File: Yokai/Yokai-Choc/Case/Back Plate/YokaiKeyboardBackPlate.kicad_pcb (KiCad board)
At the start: 2 copper layers, 161.8 x 114.7 mm, 6 parts

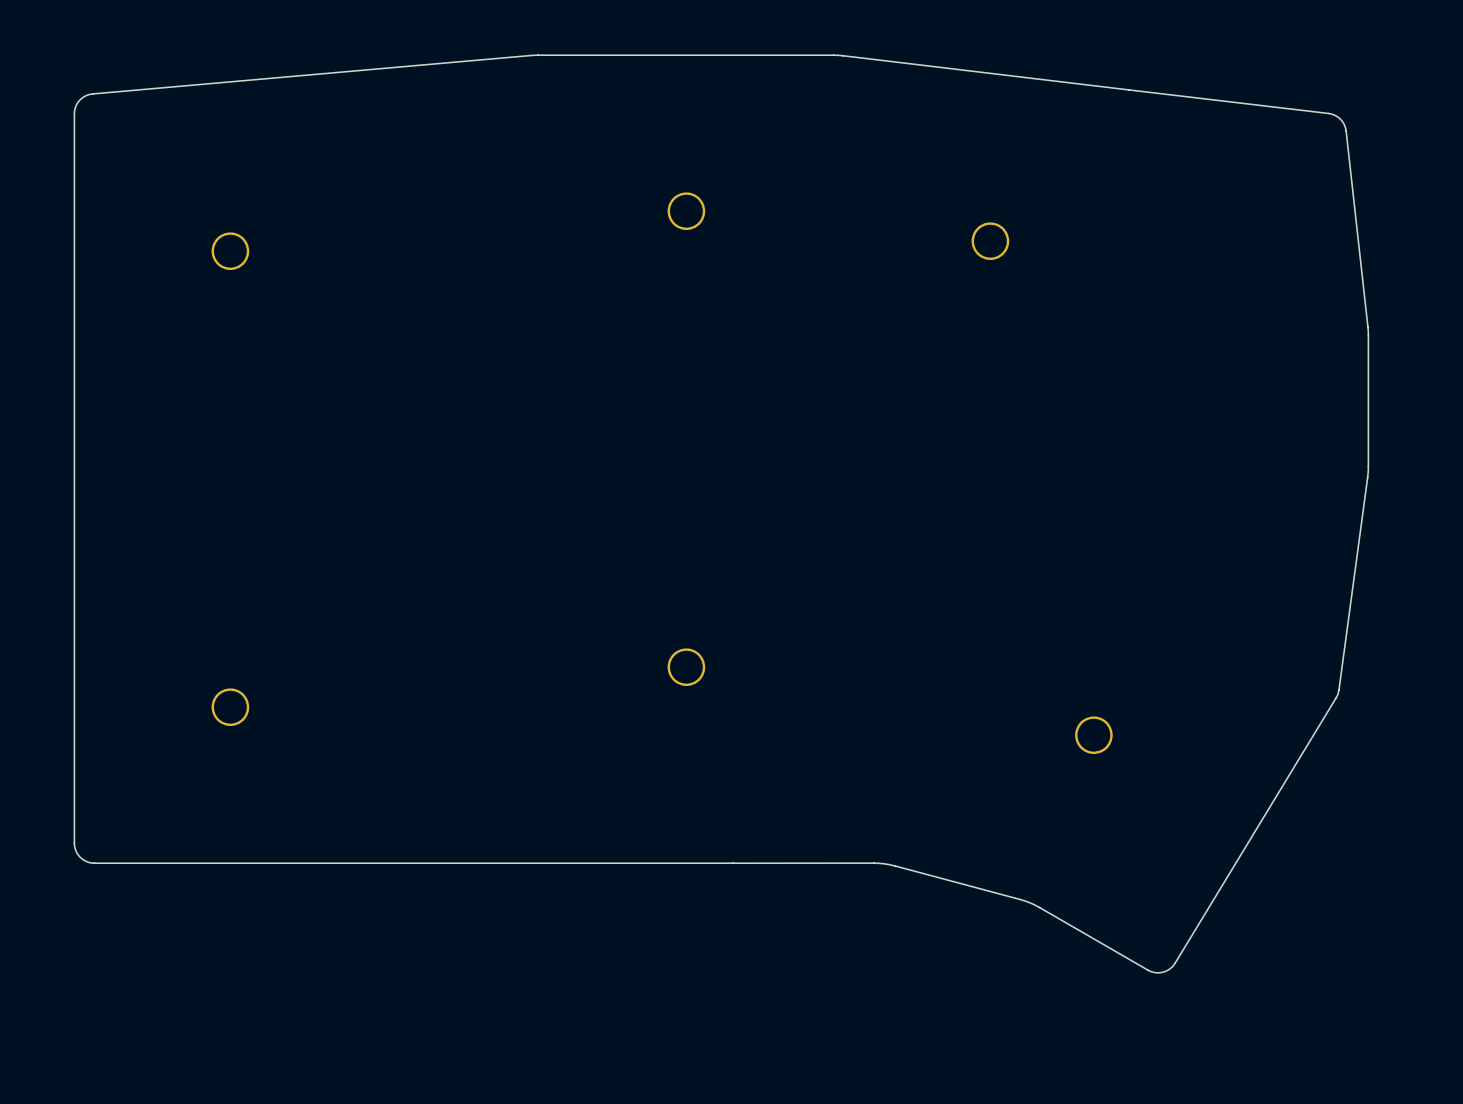
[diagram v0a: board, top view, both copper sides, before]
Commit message: Add files via upload
*Increased pinky stagger
*Inverted stabilizer cutouts
*Added additional thumb key
*Minor footprint changes
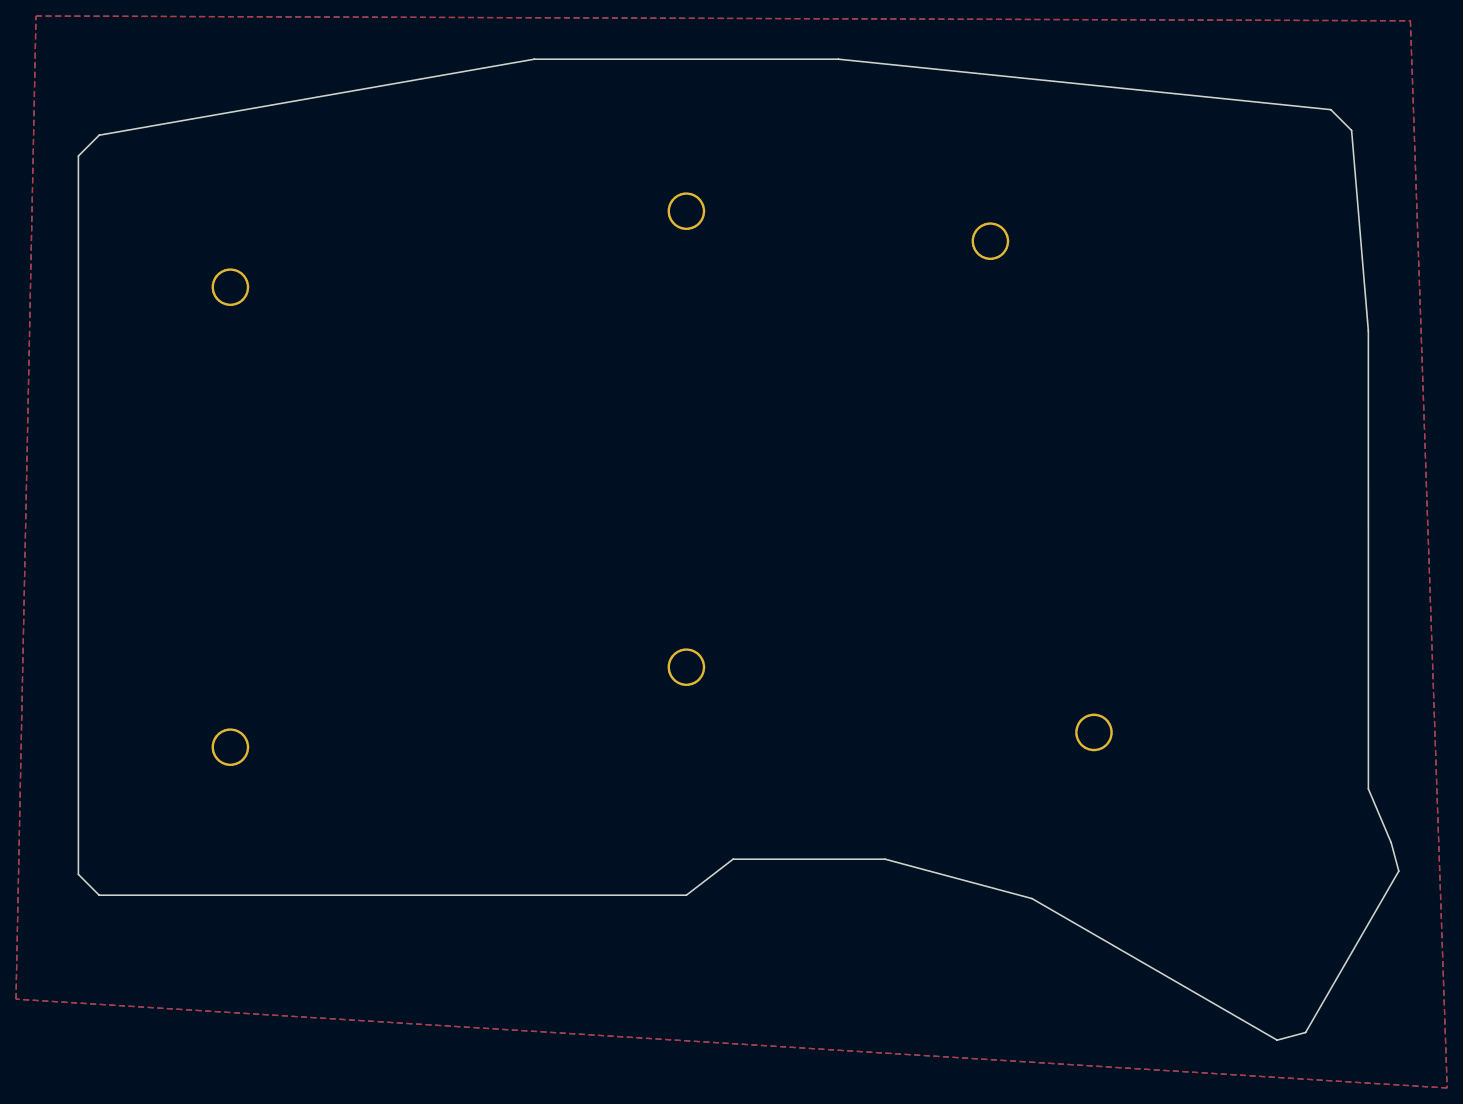
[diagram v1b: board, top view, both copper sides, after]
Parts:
- removed the TH5 at (186.9, 119.5)
- removed the TH5 at (79.0, 116.0)
- removed the TH5 at (79.0, 59.0)
- added TH5: HOLE, kbd:HOLE_M2_TH, F.Cu at (186.9, 119.2)
- added TH5: HOLE, kbd:HOLE_M2_TH, F.Cu at (79.0, 121.0)
- added TH5: HOLE, kbd:HOLE_M2_TH, F.Cu at (79.0, 63.5)
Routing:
- added copper zone on B.Cu, net (none)
- added copper zone on F.Cu, net (none)
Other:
- board size 161.8 x 114.7 mm -> 165.1 x 122.6 mm
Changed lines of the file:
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@@
   (general
     (thickness 1.6)
-    (drawings 30)
+    (drawings 18)
     (tracks 0)
     (zones 0)
@@
   )
   (module kbd:HOLE_M2_TH (layer F.Cu)
-    (at 186.936576 119.50096)
+    (at 186.947906 119.154041)
     (fp_text reference TH5 (at 0 -2.54) (layer F.SilkS) hide
       (effects (font (size 0.29972 0.29972) (thickness 0.0762)))
@@
   )
   (module kbd:HOLE_M2_TH (layer F.Cu)
-    (at 79 116)
-    (fp_text reference TH5 (at 0 -2.54) (layer F.SilkS) hide
-      (effects (font (size 0.29972 0.29972) (thickness 0.0762)))
-    )
-    (fp_text value HOLE (at 0 2.54) (layer F.SilkS) hide
-      (effects (font (size 0.29972 0.29972) (thickness 0.0762)))
-    )
-    (pad "" thru_hole circle (at 0 0 90) (size 4.7 4.7) (drill 4.1) (layers *.Cu *.Mask Dwgs.User)
-      (clearance 0.3))
-  )
-  (module kbd:HOLE_M2_TH (layer F.Cu)
-    (at 79 59)
-    (fp_text reference TH5 (at 0 -2.54) (layer F.SilkS) hide
-      (effects (font (size 0.29972 0.29972) (thickness 0.0762)))
-    )
-    (fp_text value HOLE (at 0 2.54) (layer F.SilkS) hide
-      (effects (font (size 0.29972 0.29972) (thickness 0.0762)))
-    )
-    (pad "" thru_hole circle (at 0 0 90) (size 4.7 4.7) (drill 4.1) (layers *.Cu *.Mask Dwgs.User)
-      (clearance 0.3))
-  )
-  (gr_circle (center 136 54) (end 137.282779 54) (layer Eco1.User) (width 0.2))
-  (gr_circle (center 186.936576 119.50096) (end 188.219356 119.50096) (layer Eco1.User) (width 0.2))
-  (gr_circle (center 136 111) (end 137.282779 111) (layer Eco1.User) (width 0.2))
-  (gr_circle (center 174 57.75) (end 175.282779 57.75) (layer Eco1.User) (width 0.2))
-  (gr_circle (center 79 116) (end 80.282779 116) (layer Eco1.User) (width 0.2))
-  (gr_circle (center 79 59) (end 80.282779 59) (layer Eco1.User) (width 0.2))
-  (gr_arc (start 215.982233 44.267766) (end 218.466903 43.991339) (angle -76.92360867) (layer Edge.Cuts) (width 0.2))
-  (gr_line (start 218.466903 43.991339) (end 221.188682 68.456026) (layer Edge.Cuts) (width 0.2))
-  (gr_line (start 216.275129 41.784983) (end 191.296693 38.83825) (layer Edge.Cuts) (width 0.2))
-  (gr_arc (start 211.25 69.561737) (end 221.25 69.561737) (angle -6.348242205) (layer Edge.Cuts) (width 0.2))
-  (gr_line (start 221.25 69.561737) (end 221.25 85.92804) (layer Edge.Cuts) (width 0.2))
-  (gr_arc (start 211.25 85.92804) (end 221.1601 87.265918) (angle -7.688527176) (layer Edge.Cuts) (width 0.2))
-  (gr_line (start 221.1601 87.265918) (end 217.569781 113.860593) (layer Edge.Cuts) (width 0.2))
-  (gr_arc (start 117.437756 44.5) (end 117.437756 34.5) (angle -5.013113755) (layer Edge.Cuts) (width 0.2))
-  (gr_line (start 61.78154 39.343724) (end 116.563918 34.538252) (layer Edge.Cuts) (width 0.2))
-  (gr_line (start 117.437756 34.5) (end 154.404509 34.5) (layer Edge.Cuts) (width 0.2))
-  (gr_arc (start 154.404509 44.5) (end 155.591281 34.570671) (angle -6.815768334) (layer Edge.Cuts) (width 0.2))
-  (gr_line (start 155.591281 34.570671) (end 191.296693 38.83825) (layer Edge.Cuts) (width 0.2))
-  (gr_arc (start 159.45792 145.496019) (end 162.04611 135.836761) (angle -15.01294376) (layer Edge.Cuts) (width 0.2))
-  (gr_line (start 177.727072 140.038462) (end 162.04611 135.836761) (layer Edge.Cuts) (width 0.2))
-  (gr_line (start 159.455661 135.49602) (end 141.838598 135.5) (layer Edge.Cuts) (width 0.2))
-  (gr_arc (start 175.138881 149.69772) (end 180.140837 141.038596) (angle -15.01294376) (layer Edge.Cuts) (width 0.2))
-  (gr_line (start 193.700875 148.871573) (end 180.140837 141.038596) (layer Edge.Cuts) (width 0.2))
-  (gr_arc (start 215.092256 113.526124) (end 217.229354 114.823356) (angle -23.5695086) (layer Edge.Cuts) (width 0.2))
-  (gr_line (start 217.229354 114.823356) (end 197.088462 148.004024) (layer Edge.Cuts) (width 0.2))
-  (gr_arc (start 62 133) (end 59.5 133) (angle -90) (layer Edge.Cuts) (width 0.2))
-  (gr_line (start 59.5 41.834161) (end 59.5 133) (layer Edge.Cuts) (width 0.2))
-  (gr_line (start 141.838598 135.5) (end 62 135.5) (layer Edge.Cuts) (width 0.2))
-  (gr_arc (start 194.951365 146.706792) (end 193.700875 148.871573) (angle -88.75490799) (layer Edge.Cuts) (width 0.2))
-  (gr_arc (start 62 41.834161) (end 61.78154 39.343724) (angle -84.98688624) (layer Edge.Cuts) (width 0.2))
+    (at 79 121)
+    (fp_text reference TH5 (at 0 -2.54) (layer F.SilkS) hide
+      (effects (font (size 0.29972 0.29972) (thickness 0.0762)))
+    )
+    (fp_text value HOLE (at 0 2.54) (layer F.SilkS) hide
+      (effects (font (size 0.29972 0.29972) (thickness 0.0762)))
+    )
+    (pad "" thru_hole circle (at 0 0 90) (size 4.7 4.7) (drill 4.1) (layers *.Cu *.Mask Dwgs.User)
+      (clearance 0.3))
+  )
+  (module kbd:HOLE_M2_TH (layer F.Cu)
+    (at 79 63.499999)
+    (fp_text reference TH5 (at 0 -2.54) (layer F.SilkS) hide
+      (effects (font (size 0.29972 0.29972) (thickness 0.0762)))
+    )
+    (fp_text value HOLE (at 0 2.54) (layer F.SilkS) hide
+      (effects (font (size 0.29972 0.29972) (thickness 0.0762)))
+    )
+    (pad "" thru_hole circle (at 0 0 90) (size 4.7 4.7) (drill 4.1) (layers *.Cu *.Mask Dwgs.User)
+      (clearance 0.3))
+  )
+  (gr_line (start 221.246826 68.971967) (end 221.25 126.219844) (layer Edge.Cuts) (width 0.2))
+  (gr_line (start 155 35) (end 216.550616 41.3067) (layer Edge.Cuts) (width 0.2))
+  (gr_line (start 219.150616 43.9067) (end 221.246826 68.971967) (layer Edge.Cuts) (width 0.2))
+  (gr_line (start 219.150616 43.9067) (end 216.550616 41.3067) (layer Edge.Cuts) (width 0.2))
+  (gr_line (start 221.25 126.219844) (end 224.098488 132.935837) (layer Edge.Cuts) (width 0.2))
+  (gr_line (start 179.191189 139.917561) (end 209.848488 157.617561) (layer Edge.Cuts) (width 0.2))
+  (gr_line (start 116.999999 35) (end 155 35) (layer Edge.Cuts) (width 0.2))
+  (gr_line (start 116.999999 35) (end 62.6 44.5) (layer Edge.Cuts) (width 0.2))
+  (gr_line (start 225.050154 136.487503) (end 224.098488 132.935837) (layer Edge.Cuts) (width 0.2))
+  (gr_line (start 213.400154 156.665895) (end 225.050154 136.487503) (layer Edge.Cuts) (width 0.2))
+  (gr_line (start 209.848488 157.617561) (end 213.400154 156.665895) (layer Edge.Cuts) (width 0.2))
+  (gr_line (start 62.6 139.5) (end 136 139.5) (layer Edge.Cuts) (width 0.2))
+  (gr_line (start 60 136.9) (end 62.6 139.5) (layer Edge.Cuts) (width 0.2))
+  (gr_line (start 60 47.1) (end 60 136.9) (layer Edge.Cuts) (width 0.2))
+  (gr_line (start 62.6 44.5) (end 60 47.1) (layer Edge.Cuts) (width 0.2))
+  (gr_line (start 136 139.5) (end 141.838598 135) (layer Edge.Cuts) (width 0.2))
+  (gr_line (start 141.838598 135) (end 160.838598 135) (layer Edge.Cuts) (width 0.2))
+  (gr_line (start 160.838598 135) (end 179.191189 139.917561) (layer Edge.Cuts) (width 0.2))
+  (zone (net 0) (net_name "") (layer F.Cu) (hatch edge 0.508)
+    (connect_pads (clearance 0.508))
+    (min_thickness 0.254)
+    (fill yes (arc_segments 32) (thermal_gap 0.508) (thermal_bridge_width 0.508))
+    (polygon
+      (pts
+        (xy 226.5 30.2) (xy 231.1 163.6) (xy 52.2 152.5) (xy 54.7 29.6)
+      )
+    )
+  )
+  (zone (net 0) (net_name "") (layer B.Cu) (hatch edge 0.508)
+    (connect_pads (clearance 0.508))
+    (min_thickness 0.254)
+    (fill yes (arc_segments 32) (thermal_gap 0.508) (thermal_bridge_width 0.508))
+    (polygon
+      (pts
+        (xy 226.5 30.2) (xy 231.1 163.6) (xy 52.2 152.5) (xy 54.7 29.6)
+      )
+    )
+  )
 )
